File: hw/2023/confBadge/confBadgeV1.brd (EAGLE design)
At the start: 96.5 x 78.7 mm, 94 parts, among them J1 SSW-103-22-F-D-VS-K-TRCON3_SS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, J2 SSW-103-22-F-D-VS-K-TRCON3_SS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, J3 TYPE-C-31-M-12, Q1 8/16/20MHz, U1 ATMEGA328, U10 WS2812-2020, U11 WS2812-2020, U12 WS2812-2020, U13 WS2812-2020, U14 WS2812-2020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

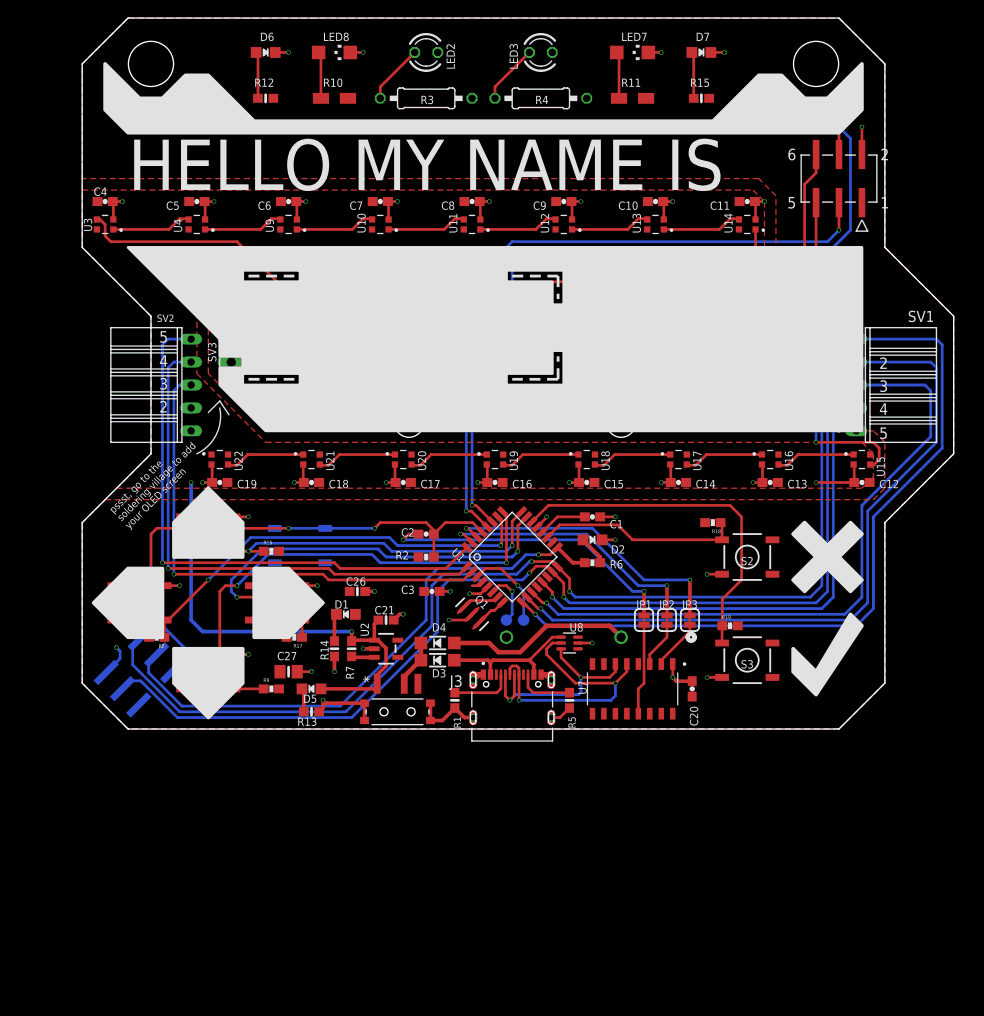
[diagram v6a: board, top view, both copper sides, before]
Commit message: All files for production with JLCPCB for both Conf and CTF Badge
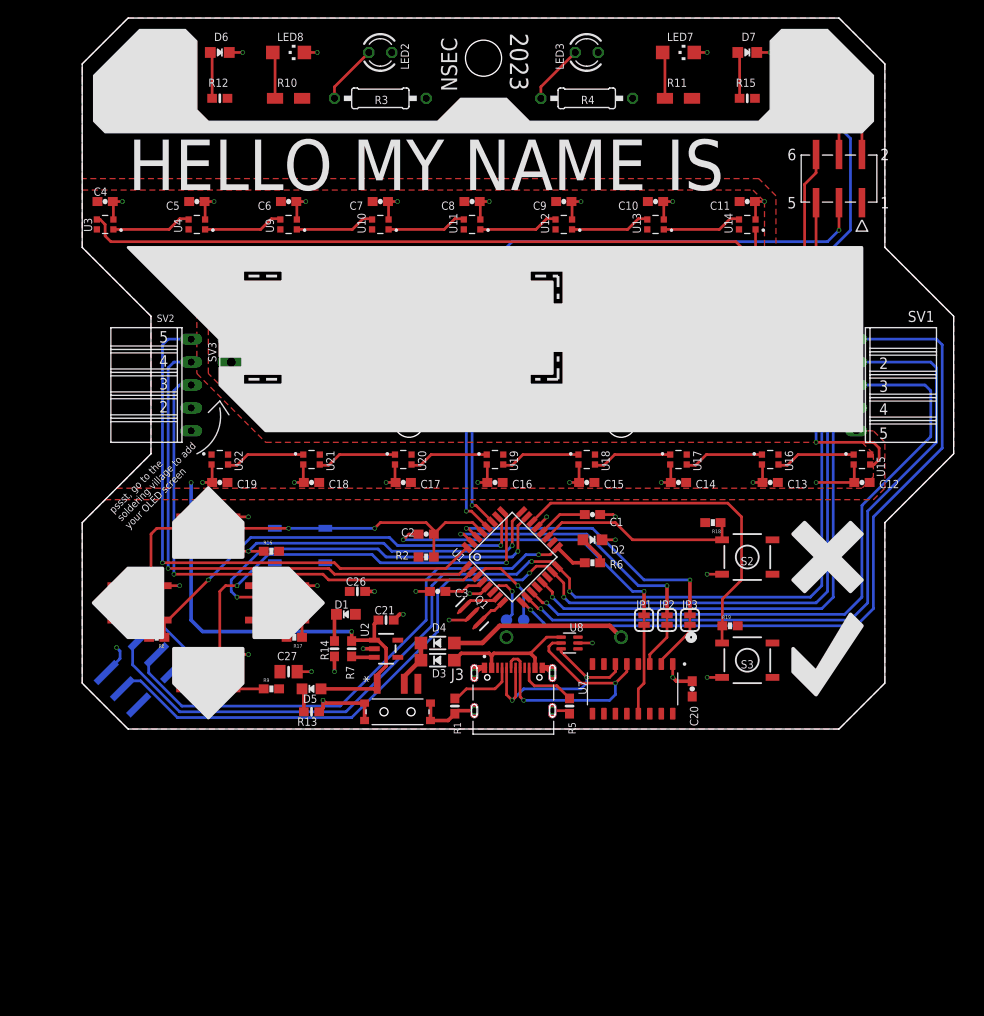
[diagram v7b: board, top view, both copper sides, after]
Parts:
- moved LED3 5.08 mm to (55.9, 74.9)
- moved LED7 5.08 mm to (66.0, 74.9)
- moved R11 5.08 mm to (66.0, 69.8)
- moved R4 5.08 mm to (55.9, 69.8)
- moved LED8 5.08 mm to (22.9, 74.9)
- moved R10 5.08 mm to (22.9, 69.8)
- moved D6 5.08 mm to (15.2, 74.9)
- moved R12 5.08 mm to (15.2, 69.8)
- moved D7 5.08 mm to (73.7, 74.9)
- moved LED2 5.08 mm to (33.0, 74.9)
- moved R15 5.08 mm to (73.7, 69.8)
- moved R3 5.08 mm to (33.0, 69.8)
- moved J3 0.77 mm to (47.8, 2.03)
- moved R1 0.63 mm to (41.3, 2.54)
- moved R5 0.63 mm to (54.0, 2.54)
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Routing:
- net 3.3V: track 4.85 -> 8.07 mm
- net USB_DN: track 25.0 -> 25.9 mm
- net VBAT: track 20.6 -> 19.8 mm
- net N$30: track 6.84 -> 7.54 mm
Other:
- board text added: "2023"
- board text added: "NSEC"

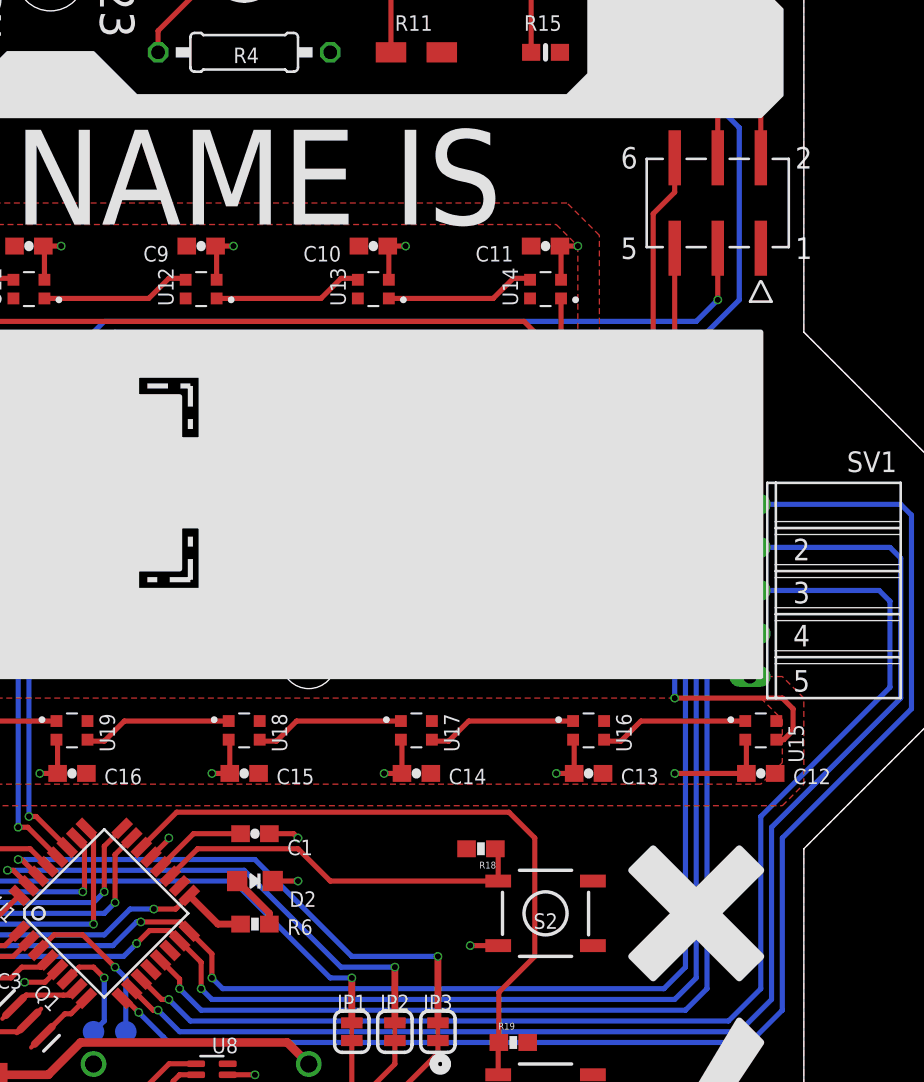
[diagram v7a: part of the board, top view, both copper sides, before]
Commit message: generated proposed factory gerber for Rizome (silkscreen still missing)
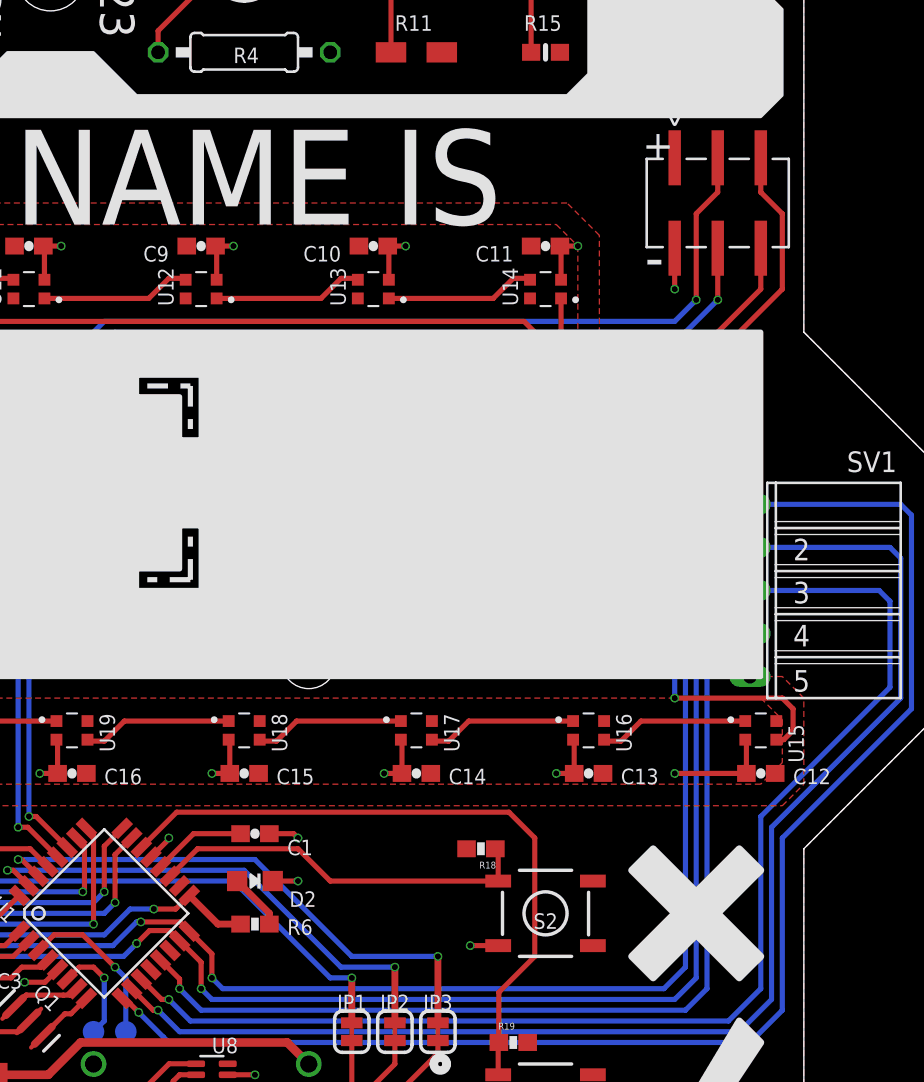
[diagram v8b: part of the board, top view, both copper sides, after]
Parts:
- turned J2 to 180 degrees
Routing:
- net SCL: track 116.5 -> 103.3 mm
- net SAO_IO1: track 136.4 -> 143.8 mm
- net SAO_IO2: track 143.3 -> 138.5 mm
- net SDA: track 102.3 -> 106.8 mm
- net GND: track 115.0 -> 114.4 mm
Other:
- board text added: "+"
- board text added: "-"
- board text added: "Connect the badge with other participants to unlock more LEDs Go to the soldering village to add a screen to your badge"
- board text added: "NORTHSEC CONFERENCE BADGE 2023"
- board text added: "QUESTS"
- board text added: "[1] [2]"
- board text removed: "Connect the badge with other participants to unlock more animations Go to the soldering village to add a screen to your badge"
- board text removed: "ISP"
- board text removed: "NORTHSEC CONF.BADGE 2023.PROTO2"
- board text removed: "QUESTS [1] [2]"
